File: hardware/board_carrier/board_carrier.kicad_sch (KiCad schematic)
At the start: 42 parts, among them J3 Conn_02x06_Top_Bottom, U1 TJA1051T-3, U2 LM78M05_TO252, U3 f042_wideband_module, U4 74LVC1G125, U5 REF3030, U6 LM2904

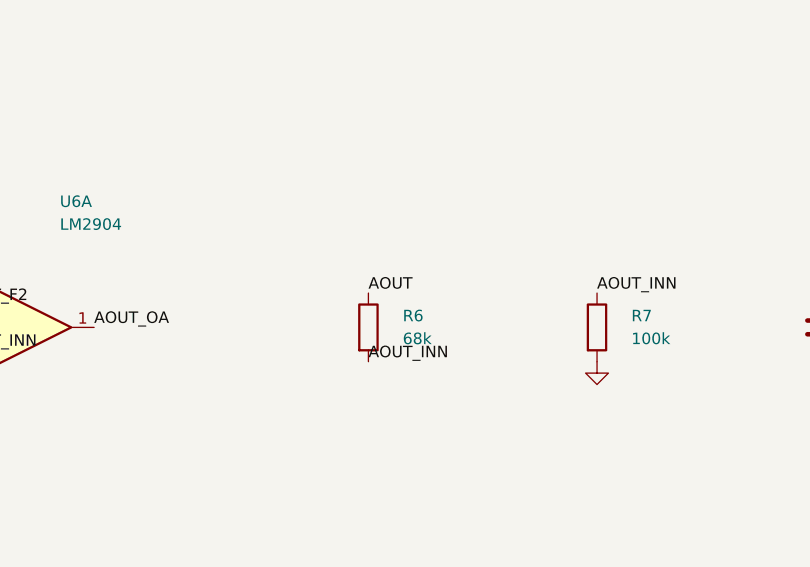
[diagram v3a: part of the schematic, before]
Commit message: board_carrier: r37: stage on the top (D9), feedback from J3-5 after R11 (C2), R9 1206 (D1), M3 holes (D8); 0 new DRC, 0 open, layout review clean. work: raw DRC advisory per D2, module-identical check
Co-Authored-By: Claude Opus 5.5 <noreply@anthropic.com>
Claude-Session: https://claude.ai/code/session_013ZVt2aLpmrSY8uzxABcZfb
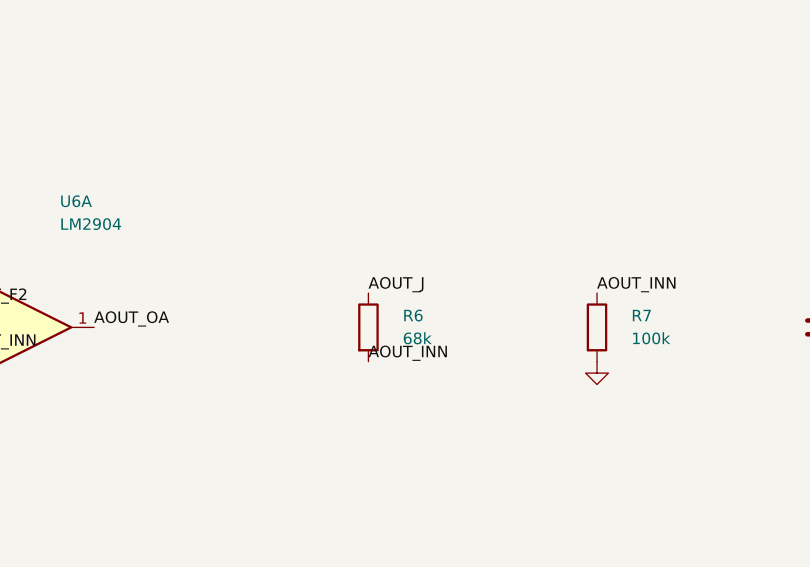
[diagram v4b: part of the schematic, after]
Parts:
- R9: footprint Resistor_SMD:R_0603_1608Metric -> Resistor_SMD:R_1206_3216Metric; LCSC C21190 -> C4410
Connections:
- net AOUT: no longer R6.1
- net AOUT_J: now also R6.1
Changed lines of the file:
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@@
 			)
 		)
-		(property "Footprint" "Resistor_SMD:R_0603_1608Metric"
+		(property "Footprint" "Resistor_SMD:R_1206_3216Metric"
 			(at 215.9 213.36 0)
 			(hide yes)
@@
 			)
 		)
-		(property "LCSC" "C21190"
+		(property "LCSC" "C4410"
 			(at 215.9 213.36 0)
 			(hide yes)
@@
 	)
 	(label "AOUT"
-		(at 279.4 168.91 0)
-		(effects
-			(font
-				(size 1.27 1.27)
-			)
-			(justify left bottom)
-		)
-	)
-	(label "AOUT"
 		(at 334.01 213.36 0)
 		(effects
@@
 		(effects
 			(font
+				(size 1.27 1.27)
+			)
+			(justify left bottom)
+		)
+	)
+	(label "AOUT_J"
+		(at 279.4 168.91 0)
+		(effects
+			(font

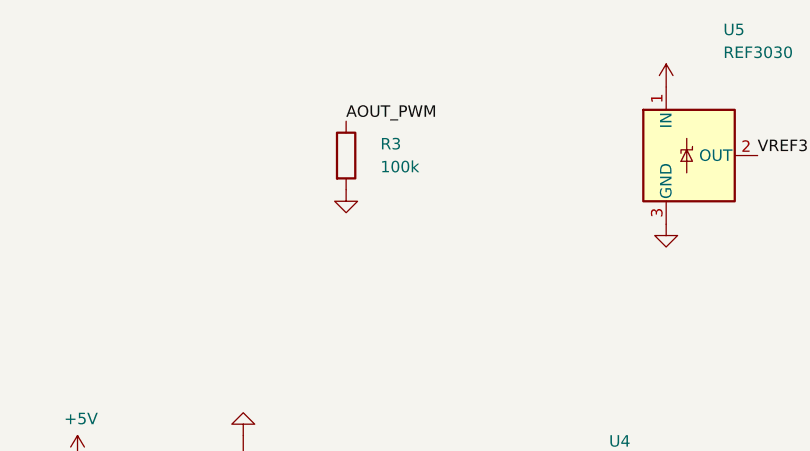
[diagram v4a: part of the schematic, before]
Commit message: board_carrier, firmware: output low from reset (outside review B1): R3 100k -> 4.7k (C25900, Basic) and PB1 pull-down in the app and bootloader board.h; invalid lambda -> 5.0 V (N1, fail lean so a closed-loop ECU adds fuel). New checks: boot_level.py; sim/full_scale_corners.sh (clamps, R9 supply, +5V tolerance; R1). EasyEDA fetch through curl (urllib now 403)
Layout unchanged (0 parts moved, same tracks and vias); 23 checks, 0 failed, 2 advisory.

Co-Authored-By: Claude Opus 5.5 <noreply@anthropic.com>
Claude-Session: https://claude.ai/code/session_013ZVt2aLpmrSY8uzxABcZfb
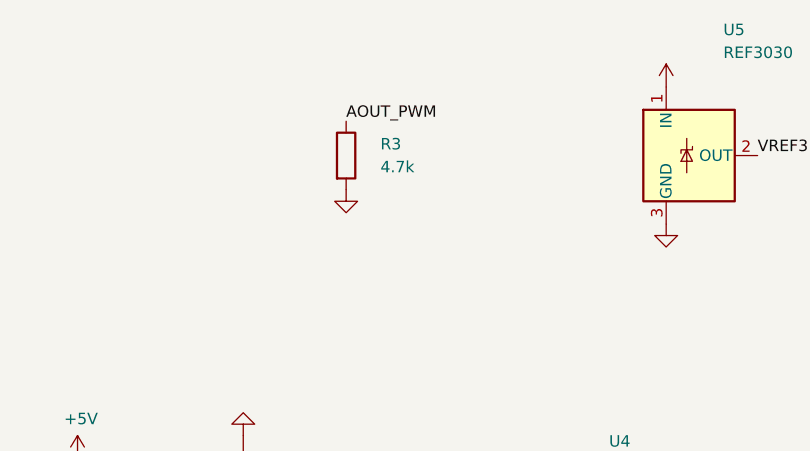
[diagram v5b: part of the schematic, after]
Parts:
- R3: value 100k -> 4.7k; LCSC C25741 -> C25900
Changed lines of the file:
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@@
 			)
 		)
-		(property "Value" "100k"
+		(property "Value" "4.7k"
 			(at 219.71 41.91 0)
 			(effects
@@
 			)
 		)
-		(property "LCSC" "C25741"
+		(property "LCSC" "C25900"
 			(at 215.9 40.64 0)
 			(hide yes)

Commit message: work, board_carrier: round 6 (Codex/Astra, PR #2) answered: stack checker and sim wrappers fixed, R9 pulse-proof
- R6-S6 (BUG): stack_estimate.py cut every loop through an indirect call, so real recursion through a
  pointer passed. Now every loop fails; five callers get a source-read target table (NARROW) cross-checked
  against their literal pools; -v no longer hangs. Regression case 4 fails on the old checker.
- R6-S8 (BUG): an aborted ngspice transient exits 0 with finite zeros and passed all three wrappers.
  sim/completed.sh: the run must reach its stop time with no abort message. 9 new fake cases fail on the
  old wrappers. Real runs: stability 25/25, load 48/48, full scale 27/27 (identical to committed).
- R6-S7: stability step at 3 ms after a settled baseline; E 0 % to 10 nF, 9.2 % / 22.4 % at 47 / 100 nF.
- R6-S3: R9 C4410 (250 mW) -> C844867 Vishay CRCW1206 HP, 0.75 W, same footprint; layout unchanged
  (one LCSC field). New check surge_budget.py (fails on C4410).
- R6-S1/S5 and TK13 doc fixes; run_all.py --report DIR for reviewers; bench test A8 (backfeed, accepted
  under C1); edge rails at the quote for C11. Round 7 hand-off and review/TASKS.md. 26 checks pass.

Co-Authored-By: Claude Opus 5.5 <noreply@anthropic.com>
Claude-Session: https://claude.ai/code/session_013ZVt2aLpmrSY8uzxABcZfb
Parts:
- R9: LCSC C4410 -> C844867
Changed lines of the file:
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@@
 			)
 		)
-		(property "LCSC" "C4410"
+		(property "LCSC" "C844867"
 			(at 215.9 213.36 0)
 			(hide yes)
